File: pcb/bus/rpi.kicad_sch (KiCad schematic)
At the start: 3 parts, among them J201 Conn_02x10_Row_Letter_First

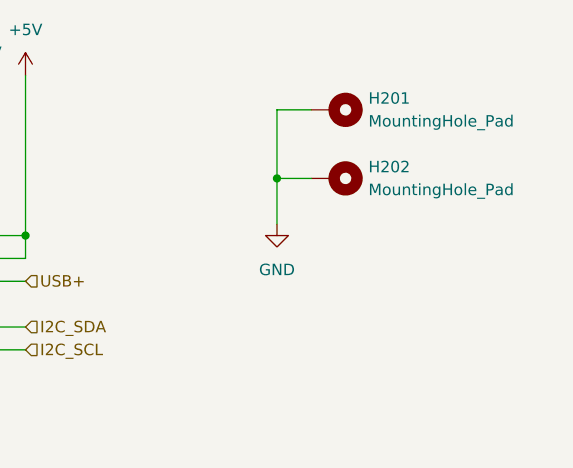
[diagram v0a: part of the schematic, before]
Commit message: update pcb size
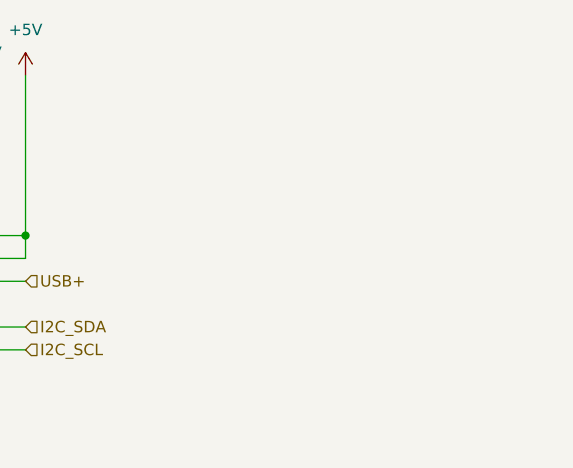
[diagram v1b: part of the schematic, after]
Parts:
- removed H201, H202: MountingHole_Pad, MountingHole:MountingHole_3.2mm_M3_Pad_Via, symbol Mechanical:MountingHole_Pad

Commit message: update bus pcb
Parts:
- added C104: 100nF, Capacitor_SMD:C_0805_2012Metric, symbol Device:C
- added U101: USBLC6-2SC6, Package_TO_SOT_SMD:SOT-666, symbol Power_Protection:USBLC6-2SC6
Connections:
- net +5V: now also C104.1, U101.5 (VBUS)
- net GND: now also C104.2, U101.2 (GND)
- net USB+: now also U101.4 (I/O2); no longer J201.a5 (Pin_a5)
- net USB-: now also U101.6 (I/O1); no longer J201.b5 (Pin_b5)
- new net NS_USB+: J201.a5 (Pin_a5), U101.3 (I/O2)
- new net NS_USB-: J201.b5 (Pin_b5), U101.1 (I/O1)
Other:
- moved on the sheet: J201

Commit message: update ALL parts
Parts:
- C104: LCSC C354365 -> C28233
- J201: MOUSER (none) -> 798-PCN1020P254DSA72
- U101: LCSC (none) -> C2827654
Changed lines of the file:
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@@
+			)
+		)
+		(property "MOUSER" "798-PCN1020P254DSA72"
+			(at 105.41 91.44 0)
+			(effects
+				(font
+					(size 1.27 1.27)
+				)
+				(hide yes)
 			)
 		)
@@
 			)
 		)
-		(property "LCSC" "C354365"
+		(property "LCSC" "C28233"
 			(at 162.56 87.63 0)
 			(effects
@@
 				)
 				(hide yes)
+			)
+		)
+		(property "MOUSER" ""
+			(at 162.56 87.63 0)
+			(effects
+				(font
+					(size 1.27 1.27)
+				)
 			)
 		)
@@
 			)
 		)
+		(property "LCSC" "C2827654"
+			(at 209.55 85.09 0)
+			(effects
+				(font
+					(size 1.27 1.27)
+				)
+			)
+		)
+		(property "MOUSER" ""
+			(at 209.55 85.09 0)
+			(effects
+				(font
+					(size 1.27 1.27)
+				)
+			)
+		)

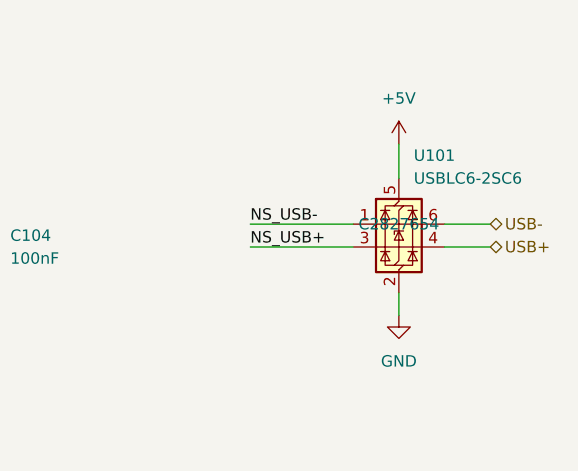
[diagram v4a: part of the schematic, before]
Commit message: move smd parts to backside - no usb length improvements
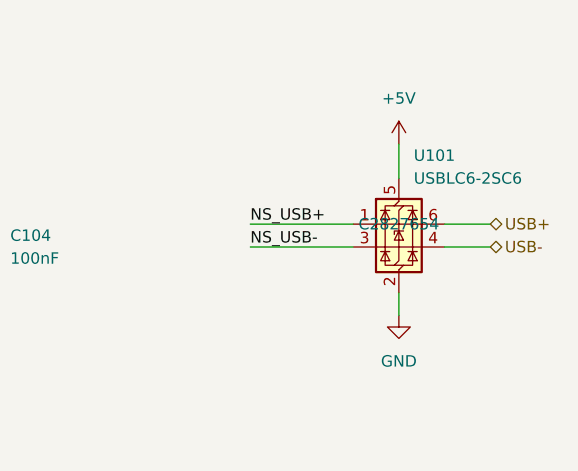
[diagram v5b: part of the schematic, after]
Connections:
- net NS_USB+: now also U101.1 (I/O1); no longer U101.3 (I/O2)
- net NS_USB-: now also U101.3 (I/O2); no longer U101.1 (I/O1)
- net USB+: now also U101.6 (I/O1); no longer U101.4 (I/O2)
- net USB-: now also U101.4 (I/O2); no longer U101.6 (I/O1)
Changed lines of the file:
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@@
 		)
 	)
-	(label "NS_USB+"
+	(label "NS_USB-"
 		(at 193.04 87.63 0)
 		(effects
@@
 		)
 	)
-	(label "NS_USB-"
+	(label "NS_USB+"
 		(at 193.04 85.09 0)
 		(effects
@@
 		)
 	)
-	(hierarchical_label "USB-"
+	(hierarchical_label "USB+"
 		(shape bidirectional)
 		(at 219.71 85.09 0)
@@
 		)
 	)
-	(hierarchical_label "USB+"
+	(hierarchical_label "USB-"
 		(shape bidirectional)
 		(at 219.71 87.63 0)

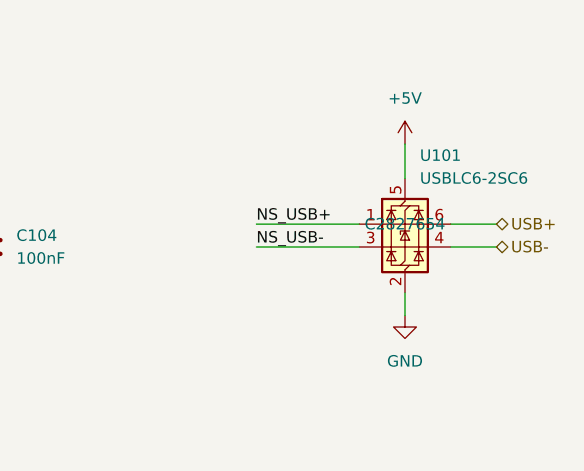
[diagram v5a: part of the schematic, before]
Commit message: fix diff pair
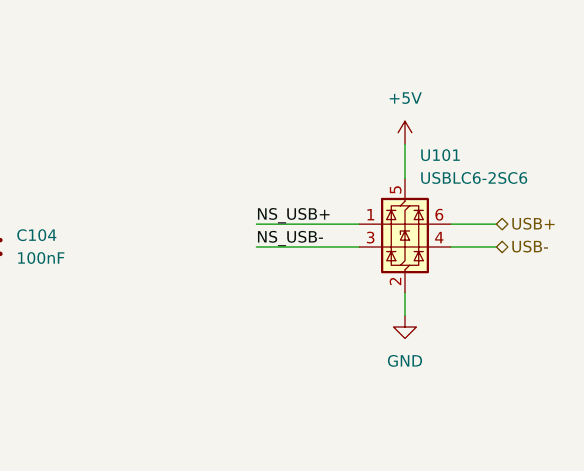
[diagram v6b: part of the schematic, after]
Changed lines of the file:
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@@
 					(size 1.27 1.27)
 				)
+				(hide yes)
 			)
 		)
@@
 					(size 1.27 1.27)
 				)
+				(hide yes)
 			)
 		)

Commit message: fix footprint in bus pcb
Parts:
- U101: footprint Package_TO_SOT_SMD:SOT-666 -> Package_TO_SOT_SMD:SOT-23-6
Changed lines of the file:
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@@
 			)
 		)
-		(property "Footprint" "Package_TO_SOT_SMD:SOT-666"
+		(property "Footprint" "Package_TO_SOT_SMD:SOT-23-6"
 			(at 210.82 91.44 0)
 			(effects
